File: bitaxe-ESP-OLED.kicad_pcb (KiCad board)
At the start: 4 copper layers, 57 x 41.6 mm, 61 parts, among them J1 Conn_01x06, J2 USB_C_Receptacle_USB2.0_16P, J3 TC2030-IDC, J4 SFV30R-4STE1HLF, Q1 SI2307, SW1 SWITCH-SPST, SW2 SWITCH-SPST, SW3 SWITCH-SPST, SW4 SWITCH-SPST, U1 RT9080-33GJ5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

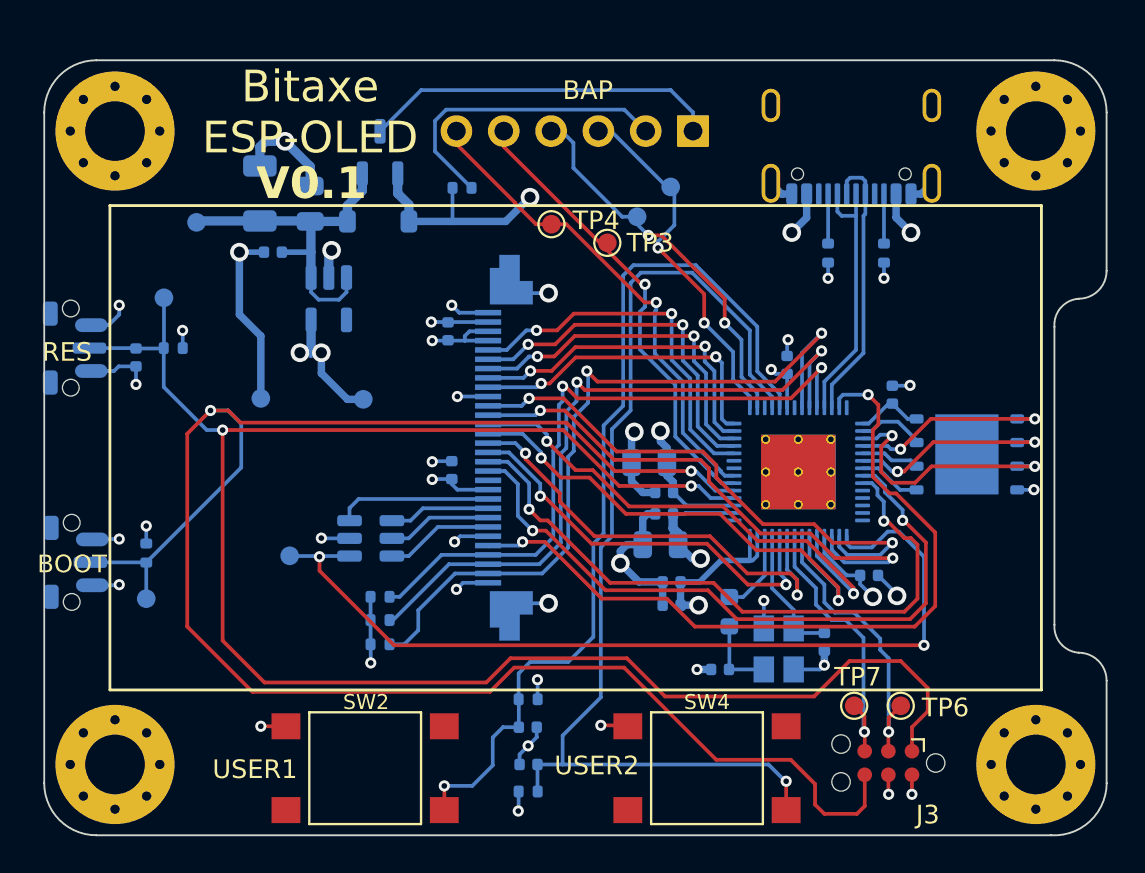
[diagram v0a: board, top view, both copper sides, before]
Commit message: more fpc room
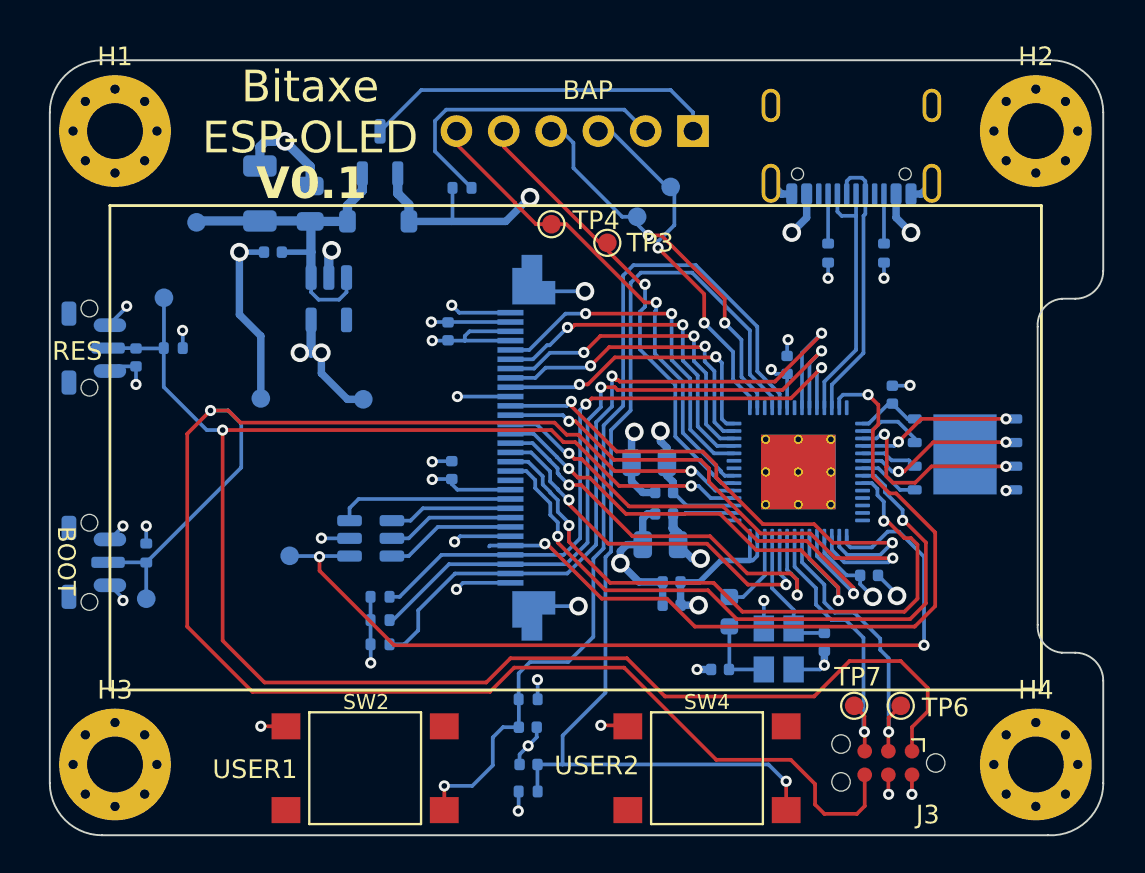
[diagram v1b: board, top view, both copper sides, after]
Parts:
- H1, H2, H3, H4: footprint MountingHole:MountingHole_3.2mm_M3_Pad_Via -> MountingHole:MountingHole_3mm_Pad_Via
- moved J4 1.20 mm to (157.2, 83.0)
- moved SW1 1.00 mm to (132.2, 77.7)
- moved SW3 0.95 mm to (132.2, 89.2)
- moved U4 0.10 mm to (179.2, 83.4)
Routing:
- net GND: track 93.6 -> 98.8 mm
- net /SPI_WP: track 13.7 -> 11.0 mm
- net /3V3: track 52.4 -> 54.8 mm
- net /SPI_CS: track 10.9 -> 8.80 mm
- net /SPI_Q: track 11.1 -> 9.10 mm
- net /LCD_D4: track 24.3 -> 22.8 mm
- net /LCD_D2: track 27.7 -> 26.3 mm
- net /LCD_D1: track 29.9 -> 28.5 mm
- net /LCD_D3: track 27.2 -> 25.8 mm
- net /LCD_DC: track 18.6 -> 17.4 mm
- net /LCD_RES: track 20.2 -> 19.0 mm
- net /LEDK4: track 8.31 -> 9.51 mm
- net /LCD_RD: track 17.1 -> 15.9 mm
- net /LEDK3: track 5.44 -> 6.64 mm
- net /LEDK2: track 5.62 -> 6.82 mm
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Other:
- board size 57 x 41.6 mm -> 56.6 x 41.6 mm

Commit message: cleanup
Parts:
- moved TP3 1.12 mm to (160.5, 73.0)
- moved J2 0.80 mm to (173.1, 66.5)
- moved C9 0.25 mm to (162.5, 83.8)
- moved J4 0.20 mm to (157.0, 83.0)
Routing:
- net /VBUS: track 37.7 -> 36.5 mm
- net /TP_RESET: track 41.7 -> 40.8 mm
- net Net-(J2-CC2): track 2.66 -> 1.86 mm
- net /USB_DP: track 14.7 -> 15.5 mm
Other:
- outline, holes or cut-outs redrawn

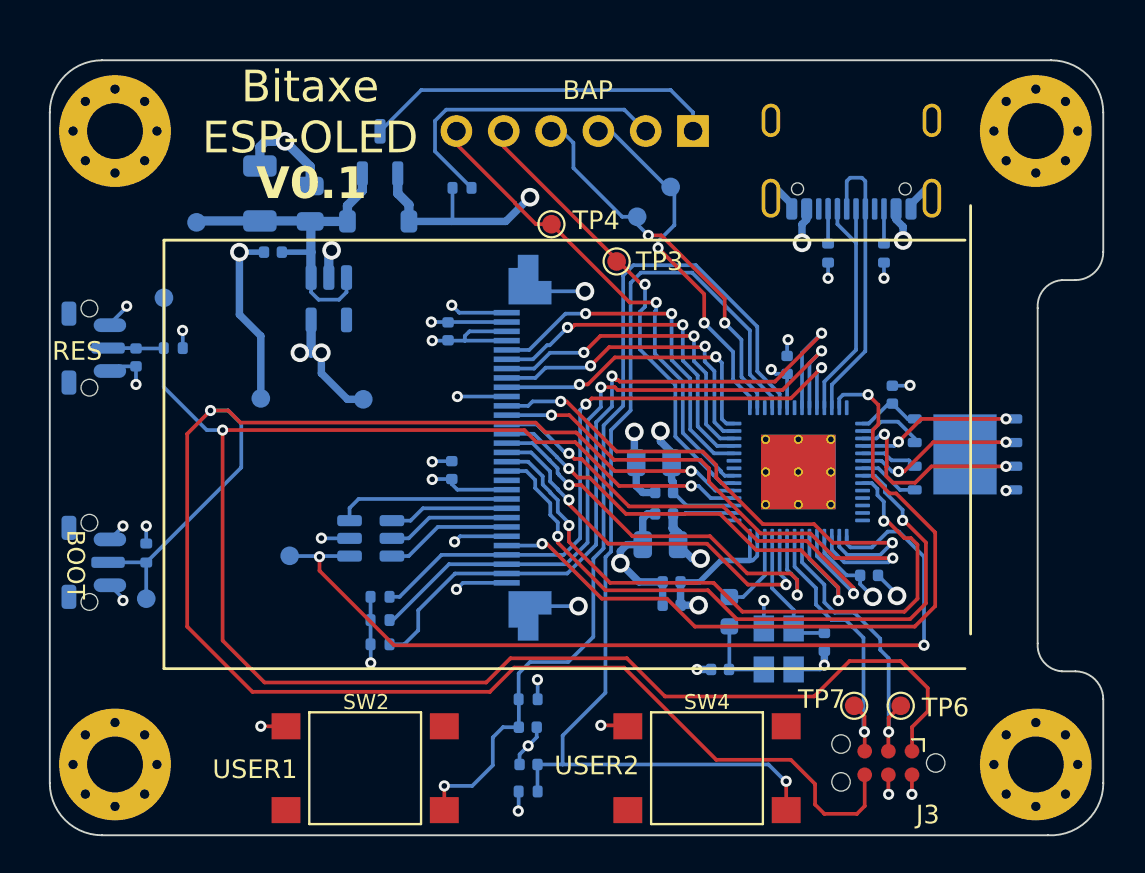
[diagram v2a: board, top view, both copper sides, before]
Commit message: link bitaxe library
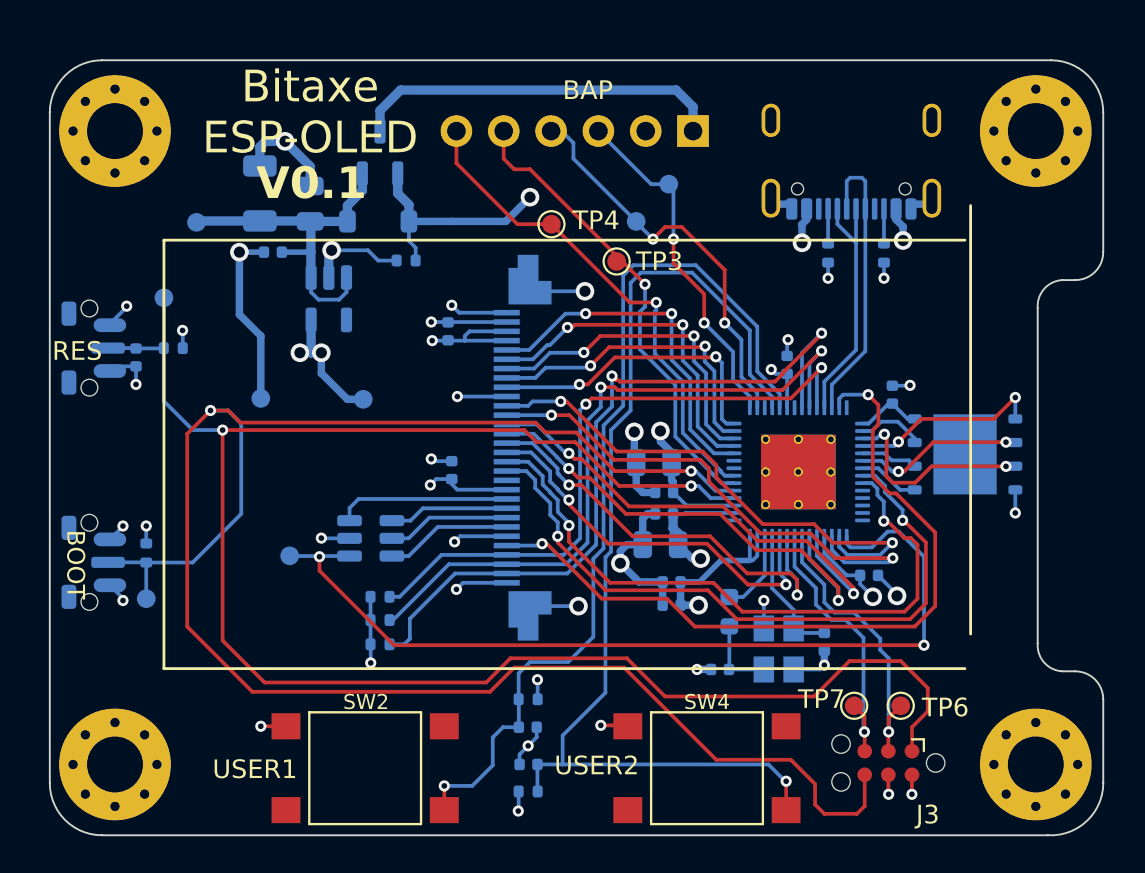
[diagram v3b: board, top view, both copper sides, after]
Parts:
- moved R7 4.92 mm to (149.2, 73.0), turned to 180 degrees
- moved TP2 0.25 mm to (161.6, 70.8)
- moved TP1 0.18 mm to (163.3, 68.8)
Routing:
- net GND: track 98.3 -> 87.4 mm
- net /SPI_CS: track 8.80 -> 10.4 mm
- net /GPIO0: track 101.6 -> 103.1 mm
- net /BAP_RX: track 20.5 -> 21.6 mm
- net /5V_BAP: track 19.2 -> 20.0 mm
- net /GPIO2: track 26.4 -> 26.9 mm
- net /BAP_TX: track 19.3 -> 18.8 mm
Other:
- board text added: "RX"
- board text added: "TX"

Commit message: moved switches
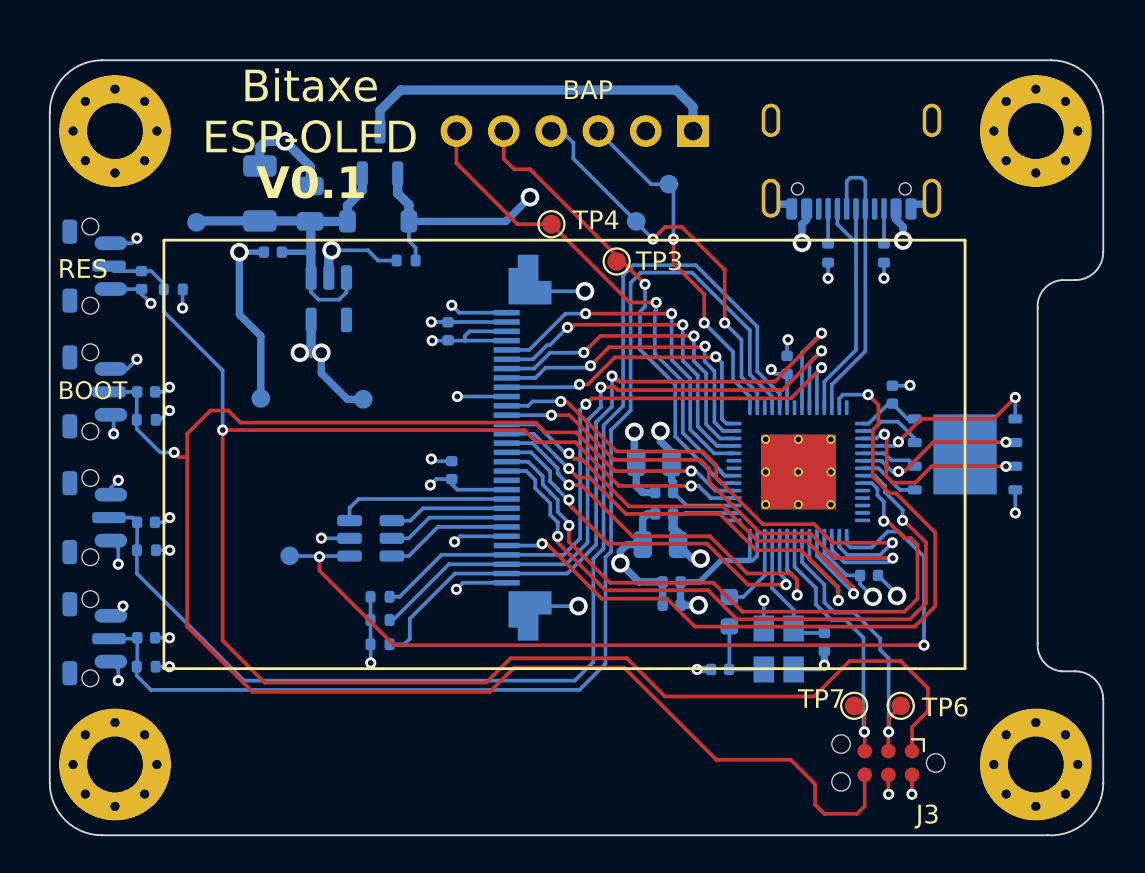
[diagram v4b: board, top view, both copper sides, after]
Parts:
- removed TP5, TP9: TestPoint, TestPoint:TestPoint_Pad_D1.0mm
- added C20: 1uF, Capacitor_SMD:C_0402_1005Metric, B.Cu at (135.2, 80.0)
- SW2, SW4: footprint bitaxe:switch-TL3301 -> bitaxe:TL3340-switch; moved to B.Cu
- moved SW4 33.8 mm to (132.2, 93.2), turned to 90 degrees
- moved C2 23.3 mm to (135.2, 87.0)
- moved R2 22.0 mm to (135.3, 88.5)
- moved C3 21.6 mm to (135.2, 93.2), turned to 0 degrees
- moved R4 21.6 mm to (135.2, 94.8), turned to 180 degrees
- moved SW2 20.0 mm to (132.2, 86.8), turned to 90 degrees
- moved SW3 9.15 mm to (132.2, 80.0)
- moved R3 7.15 mm to (135.2, 81.5), turned to 180 degrees
- moved SW1 4.40 mm to (132.2, 73.2)
- moved C1 4.16 mm to (135.0, 74.0)
- moved R1 3.15 mm to (136.7, 74.5)
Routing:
- net /UI1: track 48.9 -> 66.7 mm, vias 1 -> 0
- net /GPIO0: track 103.1 -> 93.0 mm
- net /UI2: track 56.7 -> 63.2 mm, vias 1 -> 0
- net GND: track 87.4 -> 89.8 mm, vias 31 -> 35
- net /RESET: track 98.9 -> 98.1 mm
- net /3V3: track 54.6 -> 54.0 mm
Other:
- board text removed: "+5V"
- board text removed: "USER1"
- board text removed: "USER2"

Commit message: tweaks
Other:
- board text added: "USR1"
- board text added: "USR2"
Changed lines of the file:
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@@
 		(tags "capacitor")
 		(property "Reference" "C20"
-			(at 2.5 -0.25 360)
+			(at 2.5 -0.25 0)
 			(layer "B.SilkS")
 			(effects
@@
 		)
 		(property "Value" "1uF"
-			(at 0 -1.16 360)
+			(at 0 -1.16 0)
 			(layer "B.Fab")
 			(effects
@@
 		)
 		(fp_text user "${REFERENCE}"
-			(at 0 0 360)
+			(at 0 0 0)
 			(layer "B.Fab")
 			(effects
@@
 		(tags "resistor")
 		(property "Reference" "R3"
-			(at 0.049999 -1.550001 270)
+			(at 0.049999 -1.550001 -90)
 			(layer "B.SilkS")
 			(effects
@@
 		(tags "capacitor")
 		(property "Reference" "C3"
-			(at 2.15 0.1 360)
+			(at 2.15 0.1 0)
 			(layer "B.SilkS")
 			(effects
@@
 		)
 		(property "Value" "1uF"
-			(at 0 -1.16 360)
+			(at 0 -1.16 0)
 			(layer "B.Fab")
 			(effects
@@
 		)
 		(fp_text user "${REFERENCE}"
-			(at 0 0 360)
+			(at 0 0 0)
 			(layer "B.Fab")
 			(effects
@@
 		)
 	)
+	(gr_text "USR2"
+		(at 130.5 93.75 0)
+		(layer "F.SilkS")
+		(effects
+			(font
+				(size 0.95 0.95)
+				(thickness 0.2)
+			)
+			(justify left bottom)
+		)
+	)
+	(gr_text "USR1"
+		(at 130.5 87.25 0)
+		(layer "F.SilkS")
+		(effects
+			(font
+				(size 0.95 0.95)
+				(thickness 0.2)
+			)
+			(justify left bottom)
+		)
+	)
 	(gr_text "Bitaxe\nESP-OLED"
 		(at 144.05 67.35 0)
@@
 	)
 	(via
-		(at 133.75 84.75)
+		(at 134 84.75)
 		(size 0.6)
 		(drill 0.3)
@@
 	)
 	(via
-		(at 134 91.5)
+		(at 134.25 91.25)
 		(size 0.6)
 		(drill 0.3)
@@
 	)
 	(segment
+		(start 133.35 85.4)
+		(end 133.35 85.52)
+		(width 0.2)
+		(layer "B.Cu")
+		(net 1)
+	)
+	(segment
 		(start 165.585 94.9)
 		(end 164.815 94.9)
@@
 	)
 	(segment
-		(start 133.35 85.15)
-		(end 133.75 84.75)
-		(width 0.2)
-		(layer "B.Cu")
-		(net 1)
-	)
-	(segment
 		(start 135.73 80)
 		(end 136.25 80)
@@
 	)
 	(segment
-		(start 133.35 85.52)
-		(end 133.35 85.15)
+		(start 169.65 77.25)
+		(end 169.7 77.2)
 		(width 0.2)
 		(layer "B.Cu")
@@
 	)
 	(segment
-		(start 169.65 77.25)
-		(end 169.7 77.2)
+		(start 133.5 81.38)
+		(end 133.35 81.23)
 		(width 0.2)
 		(layer "B.Cu")
@@
 	)
 	(segment
-		(start 133.5 81.38)
-		(end 133.35 81.23)
+		(start 134.25 91.25)
+		(end 133.48 92.02)
+		(width 0.2)
+		(layer "B.Cu")
+		(net 1)
+	)
+	(segment
+		(start 133.48 92.02)
+		(end 133.35 92.02)
 		(width 0.2)
 		(layer "B.Cu")
@@
 	)
 	(segment
+		(start 134 84.75)
+		(end 133.35 85.4)
+		(width 0.2)
+		(layer "B.Cu")
+		(net 1)
+	)
+	(segment
 		(start 161.9 85.4)
 		(end 162.57 85.4)
@@
 	)
 	(segment
-		(start 133.48 92.02)
-		(end 134 91.5)
-		(width 0.2)
-		(layer "B.Cu")
-		(net 1)
-	)
-	(segment
 		(start 152.05 75.75)
 		(end 151.65 75.35)
@@
 		(width 0.2)
 		(layer "B.Cu")
-		(net 1)
-	)
-	(segment
-		(start 133.35 92.02)
-		(end 133.48 92.02)
-		(width 0.2)
-		(layer "B.Cu")

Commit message: v0.3
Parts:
- removed H1, H2: MountingHole, MountingHole:MountingHole_3mm_Pad_Via
- J1: footprint Connector_PinHeader_2.54mm:PinHeader_1x06_P2.54mm_Vertical -> Connector_PinSocket_1.27mm:PinSocket_2x03_P1.27mm_Vertical_SMD
- moved J1 6.60 mm to (158.0, 66.0)
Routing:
- net /5V_BAP: track 20.0 -> 15.3 mm, vias 0 -> 2
- net /GPIO2: track 26.9 -> 23.1 mm, vias 1 -> 2
- net /BAP_TX: track 18.8 -> 21.8 mm
- net GND: track 90.3 -> 92.1 mm, vias 35 -> 36
- net /BAP_RX: track 21.6 -> 20.1 mm
- net /GPIO1: track 25.1 -> 25.5 mm, vias 1 -> 2
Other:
- outline, holes or cut-outs redrawn
- board text added: "V0.3"
- board text removed: "V0.1"

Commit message: Expand copper pour underneath MCU
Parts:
- U3: footprint Package_TO_SOT_SMD:SOT-23-6 -> bitaxe:SOT-23-6
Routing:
- net /TP_RESET: track 40.8 -> 46.9 mm
- net /I2C_SCL: track 34.6 -> 38.7 mm
- net /I2C_SCK: track 37.1 -> 38.7 mm
- net /LCD_D0: track 28.2 -> 29.3 mm
- net /LCD_D1: track 28.7 -> 29.5 mm
- net /3V3: track 54.0 -> 54.8 mm
- net GND: track 92.1 -> 92.8 mm
- net /SPI_WP: track 11.0 -> 11.7 mm
- added copper zone on F.Cu, net GND
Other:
- board text added: "V0.4"
- board text removed: "V0.3"
